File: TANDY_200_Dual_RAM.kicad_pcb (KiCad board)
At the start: 2 copper layers, 35.6 x 25.4 mm, 5 parts, among them J1 Conn_01x01_Male, J2 TANDY_26-3688, U1 628128_SOP32, U2 74LVC1G08

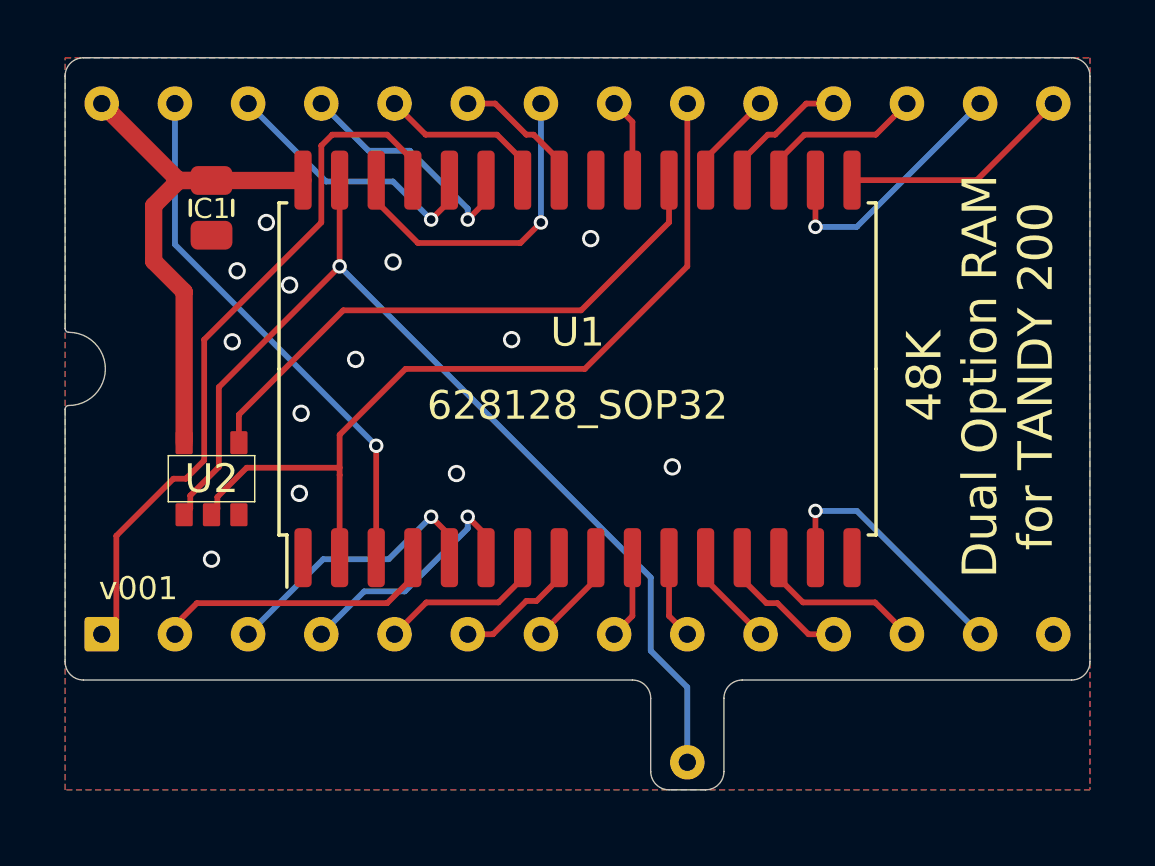
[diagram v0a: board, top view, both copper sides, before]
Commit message: symmetrical part placement
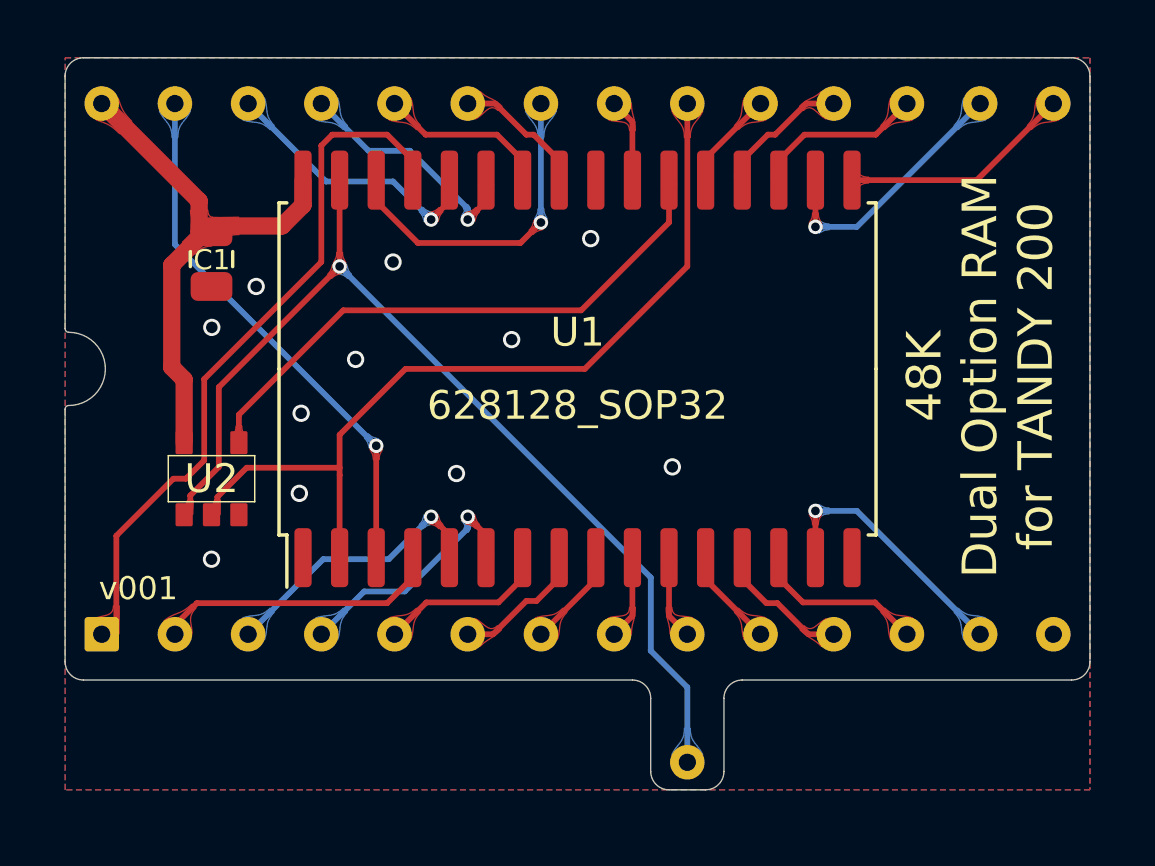
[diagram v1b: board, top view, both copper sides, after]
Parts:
- moved C1 1.78 mm to (134.6, 95.2)
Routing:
- net GND: vias 13 -> 11

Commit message: board outlines, ground planes
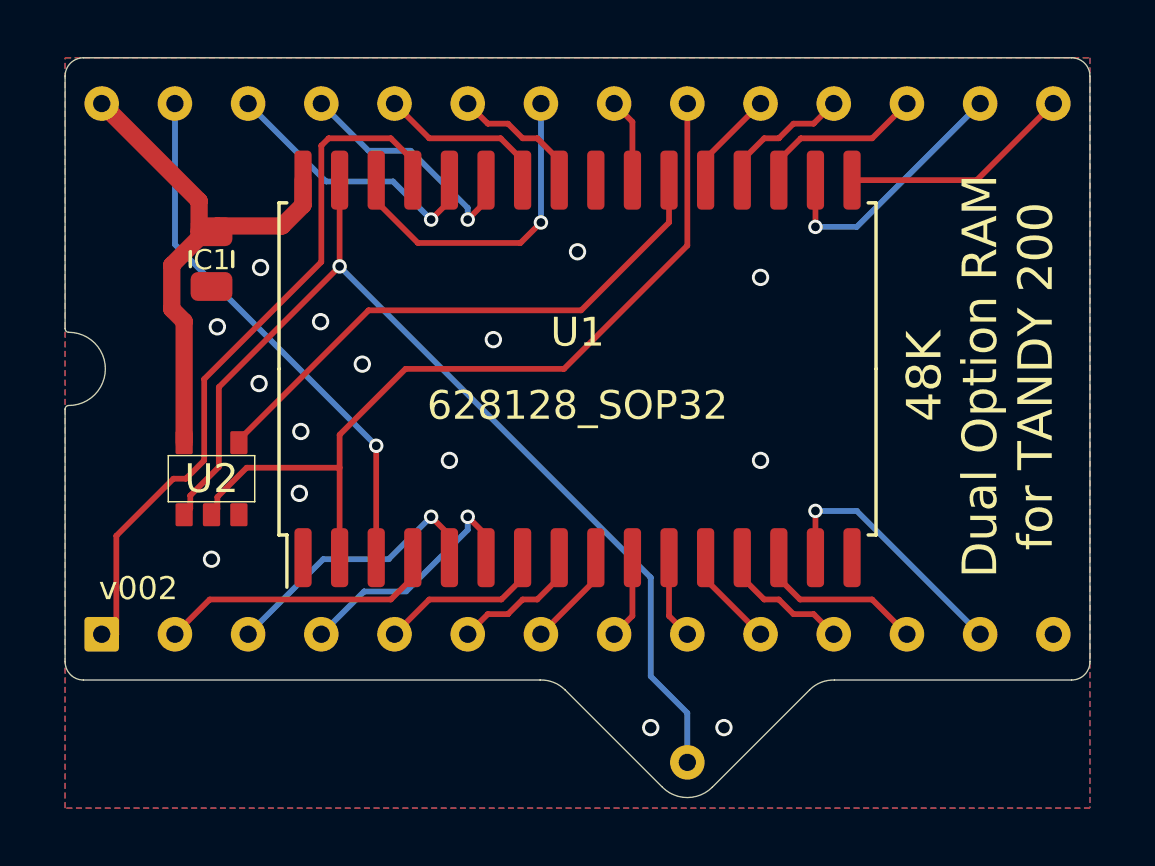
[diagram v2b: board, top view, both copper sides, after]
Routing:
- net /~{CE}: track 20.1 -> 19.6 mm
- net GND: vias 11 -> 15
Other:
- board size 35.6 x 25.4 mm -> 35.6 x 25.7 mm
- board text removed: "Row spacing is 725mils, not 700."

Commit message: ground paths, footprints, sch symbols
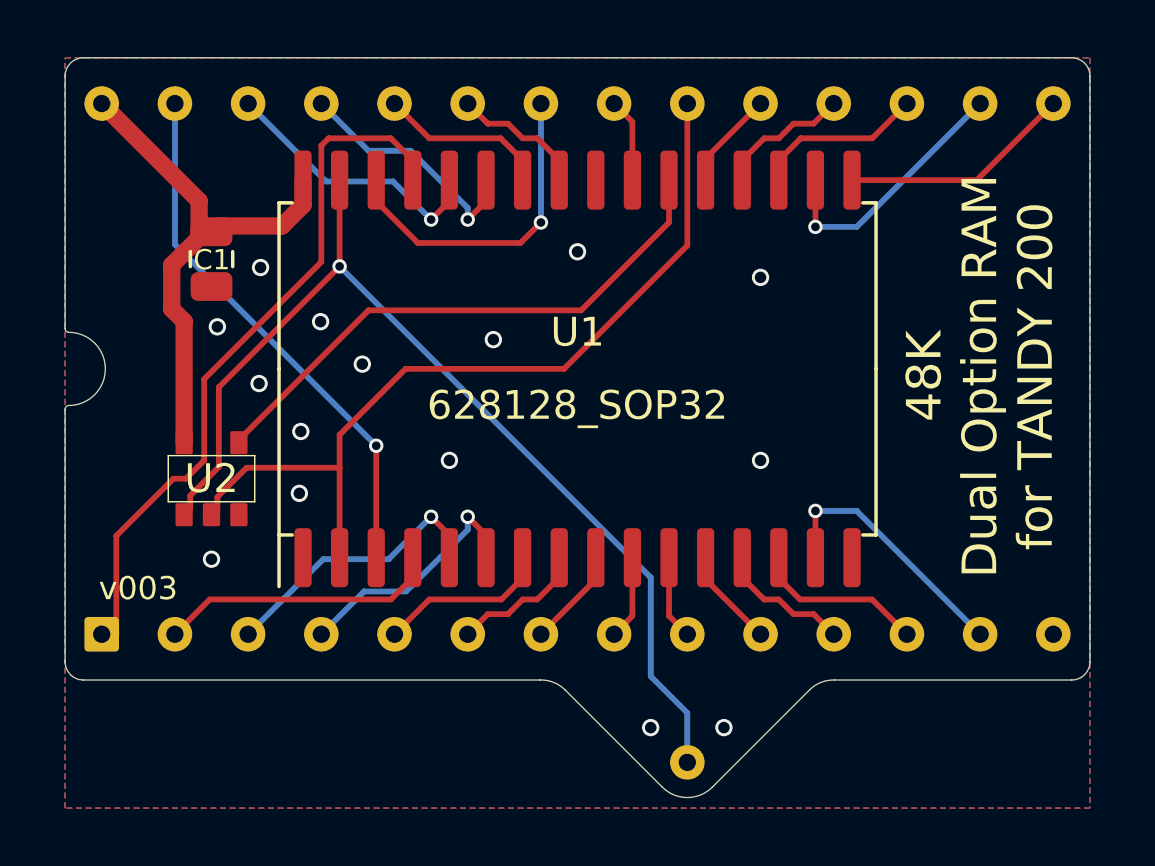
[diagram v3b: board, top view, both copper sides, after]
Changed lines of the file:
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@@
   (title_block
     (title "TANDY 200 Dual RAM")
-    (date "2022-09-17")
-    (rev "002")
+    (date "2022-09-21")
+    (rev "003")
     (company "b.kenyon.w@gmail.com")
     (comment 1 "github.com/bkw777/TANDY_200_RAM")
@@
     (at 151.13 112.7125)
     (descr "tht pin")
-    (property "Sheetfile" "TANDY_200_DUAL_RAM_soic.kicad_sch")
+    (property "Sheetfile" "TANDY_200_Dual_RAM.kicad_sch")
     (property "Sheetname" "")
     (attr through_hole)
@@
     (descr "Capacitor SMD 0805 (2012 Metric), square (rectangular) end terminal, IPC_7351 nominal, (Body size source: IPC-SM-782 page 76, https://www.pcb-3d.com/wordpress/wp-content/uploads/ipc-sm-782a_amendment_1_and_2.pdf, https://docs.google.com/spreadsheets/d/1BsfQQcO9C6DZCsRaXUlFlo91Tg2WpOkGARC1WS5S8t0/edit?usp=sharing), generated with kicad-footprint-generator")
     (tags "capacitor")
-    (property "Sheetfile" "TANDY_200_DUAL_RAM_soic.kicad_sch")
+    (property "Sheetfile" "TANDY_200_Dual_RAM.kicad_sch")
     (property "Sheetname" "")
     (attr smd)
@@
     (descr "SSOP, 32 Pin (http://www.issi.com/WW/pdf/61-64C5128AL.pdf), generated with kicad-footprint-generator ipc_gullwing_generator.py")
     (tags "SSOP SO SOP SOIC 32")
-    (property "Sheetfile" "TANDY_200_DUAL_RAM_soic.kicad_sch")
+    (property "Sheetfile" "TANDY_200_Dual_RAM.kicad_sch")
     (property "Sheetname" "")
     (attr smd)
@@
       (effects (font (size 1 1) (thickness 0.15)))
     )
-    (fp_line (start 0 -10.3575) (end -5.7625 -10.3575) (layer "F.SilkS") (width 0.12))
-    (fp_line (start -5.7625 -10.085) (end -7.575 -10.085) (layer "F.SilkS") (width 0.12))
-    (fp_line (start 5.7625 10.3575) (end 5.7625 10.085) (layer "F.SilkS") (width 0.12))
+    (fp_line (start 0 -10.3575) (end 5.7625 -10.3575) (layer "F.SilkS") (width 0.12))
+    (fp_line (start 5.7625 -9.9) (end 5.7625 -10.3575) (layer "F.SilkS") (width 0.12))
+    (fp_line (start 0 -10.3575) (end -7.55 -10.3575) (layer "F.SilkS") (width 0.12))
+    (fp_line (start 0 10.3575) (end -5.7625 10.3575) (layer "F.SilkS") (width 0.12))
+    (fp_line (start -5.7625 10.3575) (end -5.7625 9.9) (layer "F.SilkS") (width 0.12))
+    (fp_line (start 5.7625 10.3575) (end 5.7625 9.9) (layer "F.SilkS") (width 0.12))
+    (fp_line (start -5.7625 -9.9) (end -5.7625 -10.3575) (layer "F.SilkS") (width 0.12))
     (fp_line (start 0 10.3575) (end 5.7625 10.3575) (layer "F.SilkS") (width 0.12))
-    (fp_line (start 0 10.3575) (end -5.7625 10.3575) (layer "F.SilkS") (width 0.12))
-    (fp_line (start 0 -10.3575) (end 5.7625 -10.3575) (layer "F.SilkS") (width 0.12))
-    (fp_line (start 5.7625 -10.3575) (end 5.7625 -10.085) (layer "F.SilkS") (width 0.12))
-    (fp_line (start -5.7625 -10.3575) (end -5.7625 -10.085) (layer "F.SilkS") (width 0.12))
-    (fp_line (start -5.7625 10.3575) (end -5.7625 10.085) (layer "F.SilkS") (width 0.12))
+    (fp_line (start -7.83 -10.5) (end -7.83 10.5) (layer "F.CrtYd") (width 0.05))
+    (fp_line (start 7.83 -10.5) (end -7.83 -10.5) (layer "F.CrtYd") (width 0.05))
+    (fp_line (start 7.83 10.5) (end 7.83 -10.5) (layer "F.CrtYd") (width 0.05))
     (fp_line (start -7.83 10.5) (end 7.83 10.5) (layer "F.CrtYd") (width 0.05))
-    (fp_line (start 7.83 10.5) (end 7.83 -10.5) (layer "F.CrtYd") (width 0.05))
-    (fp_line (start 7.83 -10.5) (end -7.83 -10.5) (layer "F.CrtYd") (width 0.05))
-    (fp_line (start -7.83 -10.5) (end -7.83 10.5) (layer "F.CrtYd") (width 0.05))
+    (fp_line (start -5.6525 -9.2475) (end -4.6525 -10.2475) (layer "F.Fab") (width 0.1))
+    (fp_line (start 5.6525 -10.2475) (end 5.6525 10.2475) (layer "F.Fab") (width 0.1))
+    (fp_line (start 5.6525 10.2475) (end -5.6525 10.2475) (layer "F.Fab") (width 0.1))
     (fp_line (start -5.6525 10.2475) (end -5.6525 -9.2475) (layer "F.Fab") (width 0.1))
-    (fp_line (start 5.6525 10.2475) (end -5.6525 10.2475) (layer "F.Fab") (width 0.1))
-    (fp_line (start 5.6525 -10.2475) (end 5.6525 10.2475) (layer "F.Fab") (width 0.1))
-    (fp_line (start -5.6525 -9.2475) (end -4.6525 -10.2475) (layer "F.Fab") (width 0.1))
     (fp_line (start -4.6525 -10.2475) (end 5.6525 -10.2475) (layer "F.Fab") (width 0.1))
     (pad "1" smd roundrect (at -6.55 -9.525 90) (size 2.05 0.6) (layers "F.Cu" "F.Paste" "F.Mask") (roundrect_rratio 0.25)
@@
     (descr "28-lead though-hole DIP, row spacing 725mils")
     (tags "THT DIP DIL 2.54mm 725mil")
-    (property "Sheetfile" "TANDY_200_DUAL_RAM_soic.kicad_sch")
+    (property "Sheetfile" "TANDY_200_Dual_RAM.kicad_sch")
     (property "Sheetname" "")
     (attr through_hole)
@@
     (descr "5-pin SOT23 package")
     (tags "SOT-23-5")
-    (property "Sheetfile" "TANDY_200_DUAL_RAM_soic.kicad_sch")
+    (property "Sheetfile" "TANDY_200_Dual_RAM.kicad_sch")
     (property "Sheetname" "")
     (attr smd)
@@
       (effects (font (size 1 1) (thickness 0.15)))
     )
-    (fp_text value "74LVC1G08" (at 0 2.9 90) (layer "F.Fab") hide
-      (effects (font (size 1 1) (thickness 0.15)))
-    )
-    (fp_text user "${REFERENCE}" (at 0 0) (layer "F.Fab") hide
+    (fp_text value "74LVC1G08" (at 0 2.9 90) (layer "F.Fab")
+      (effects (font (size 1 1) (thickness 0.15)))
+    )
+    (fp_text user "${REFERENCE}" (at 0 0 180) (layer "F.Fab")
       (effects (font (size 0.5 0.5) (thickness 0.075)))
     )
+    (fp_line (start -0.8 1.5) (end 0.8 1.5) (layer "F.SilkS") (width 0.0508))
+    (fp_line (start 0.8 -1.5) (end -0.8 -1.5) (layer "F.SilkS") (width 0.0508))
     (fp_line (start -0.8 -1.5) (end -0.8 1.5) (layer "F.SilkS") (width 0.0508))
     (fp_line (start 0.8 1.5) (end 0.8 -1.5) (layer "F.SilkS") (width 0.0508))
-    (fp_line (start -0.8 1.5) (end 0.8 1.5) (layer "F.SilkS") (width 0.0508))
-    (fp_line (start 0.8 -1.5) (end -0.8 -1.5) (layer "F.SilkS") (width 0.0508))
+    (fp_line (start -1.9 -1.75) (end 1.9 -1.75) (layer "F.CrtYd") (width 0.05))
+    (fp_line (start 1.9 1.75) (end -1.9 1.75) (layer "F.CrtYd") (width 0.05))
+    (fp_line (start -1.9 1.75) (end -1.9 -1.75) (layer "F.CrtYd") (width 0.05))
+    (fp_line (start 1.9 -1.75) (end 1.9 1.75) (layer "F.CrtYd") (width 0.05))
+    (fp_line (start 0.9 1.55) (end -0.9 1.55) (layer "F.Fab") (width 0.1))
+    (fp_line (start -0.9 -0.9) (end -0.25 -1.55) (layer "F.Fab") (width 0.1))
+    (fp_line (start 0.9 -1.55) (end 0.9 1.55) (layer "F.Fab") (width 0.1))
     (fp_line (start 0.9 -1.55) (end -0.25 -1.55) (layer "F.Fab") (width 0.1))
     (fp_line (start -0.9 -0.9) (end -0.9 1.55) (layer "F.Fab") (width 0.1))
-    (fp_line (start -0.9 -0.9) (end -0.25 -1.55) (layer "F.Fab") (width 0.1))
-    (fp_line (start 0.9 1.55) (end -0.9 1.55) (layer "F.Fab") (width 0.1))
-    (fp_line (start 0.9 -1.55) (end 0.9 1.55) (layer "F.Fab") (width 0.1))
     (pad "1" smd roundrect (at -1.25 -0.95 90) (size 0.8 0.6) (layers "F.Cu" "F.Paste" "F.Mask") (roundrect_rratio 0.1)
       (net 25 "/~{BANK5}") (pintype "input"))
